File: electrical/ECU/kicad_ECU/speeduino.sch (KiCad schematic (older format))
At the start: 0 parts

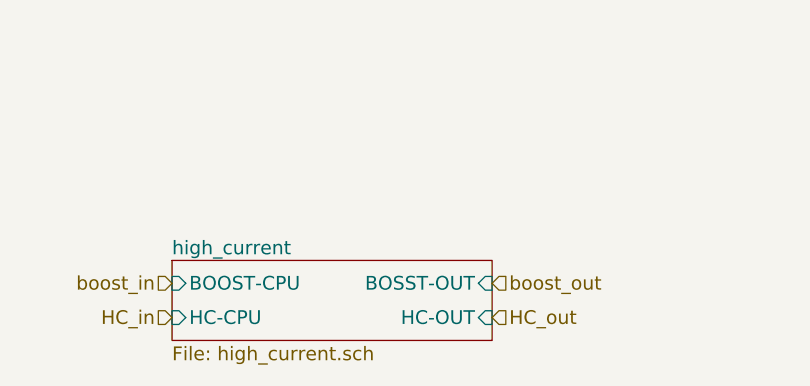
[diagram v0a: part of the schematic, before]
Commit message: fixed some naming errors and initial round of double checking
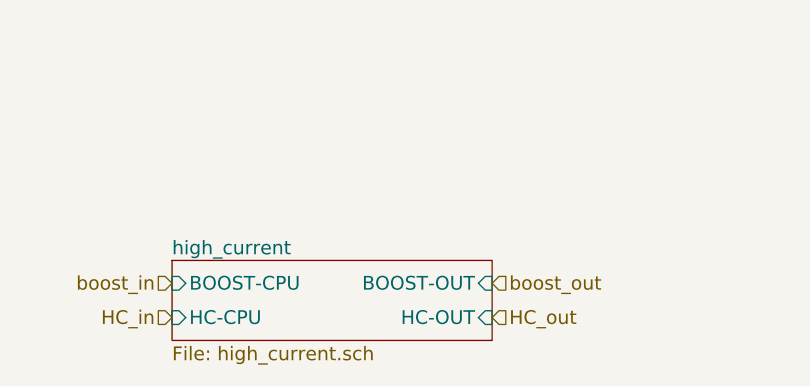
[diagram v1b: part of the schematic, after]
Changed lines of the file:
@@
 $Descr A4 11693 8268
 encoding utf-8
-Sheet 11 33
+Sheet 12 33
 Title "Speeduino"
 Date ""
@@
 F3 "HC-CPU" I L 3250 7100 60
 F4 "HC-OUT" I R 4650 7100 60
-F5 "BOSST-OUT" I R 4650 6950 60
+F5 "BOOST-OUT" I R 4650 6950 60
 $EndSheet
 $Sheet
@@
 MAP2_CPU
 $Comp
-L Earth #PWR?
+L Earth #PWR39
 U 1 1 597911A5
 P 8650 5450
-F 0 "#PWR?" H 8650 5200 50  0001 C CNN
+F 0 "#PWR39" H 8650 5200 50  0001 C CNN
 F 1 "Earth" H 8650 5300 50  0001 C CNN
 F 2 "" H 8650 5450 50  0001 C CNN
